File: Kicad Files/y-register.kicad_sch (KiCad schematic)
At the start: 20 parts, among them U1 74LS245, U2 74LS173, U3 74LS173

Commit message: updated library
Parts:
- removed D25, D26, D27, D28, D29, D30, D31, D32: RED, LED_THT:LED_D5.0mm, symbol 8bit-computer-rescue:LED_ALT-Device
- removed R25, R26, R27, R28, R29, R30, R31, R32: R, Resistor_THT:R_Axial_DIN0207_L6.3mm_D2.5mm_P7.62mm_Horizontal, symbol Device:R
- removed U1: 74LS245, Package_DIP:DIP-20_W7.62mm, symbol 8bit-computer-rescue:74LS245-8bit-computer-rescue
- removed U2, U3: 74LS173, Package_DIP:DIP-16_W7.62mm, symbol 8bit-computer-rescue:74LS173-8bit-computer-rescue
- added D33, D34, D35, D36, D37, D38, D39, D40: LED, symbol Device:LED
- added R33, R34, R35, R36, R37, R38, R39, R40: R_Small, symbol Device:R_Small
- added U1: 74HC245, symbol 74xx:74HC245
- added U2, U3: 74LS173, symbol 74xx:74LS173
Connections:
- net BUS_0: now also U1.11 (B7), U3.11 (D3)
- net BUS_1: now also U1.12 (B6), U3.12 (D2)
- net BUS_2: now also U1.13 (B5), U3.13 (D1)
- net BUS_3: now also U1.14 (B4), U3.14 (D0)
- net BUS_4: now also U1.15 (B3), U2.11 (D3)
- net BUS_5: now also U1.16 (B2), U2.12 (D2)
- net BUS_6: now also U1.17 (B1), U2.13 (D1)
- net BUS_7: now also U1.18 (B0), U2.14 (D0)
- net CLK: now also U2.7 (Cp), U3.7 (Cp)
- net CLR: now also U2.15 (Mr), U3.15 (Mr)
- net GND: now also R33.2, R34.2, R35.2, R36.2, R37.2, R38.2, R39.2, R40.2, U1.10 (GND), U2.1 (Oe1), U2.16 (VCC), U2.2 (Oe2), U3.1 (Oe1), U3.16 (VCC), U3.2 (Oe2)
- net VCC: now also U1.1 (A->B), U1.20 (VCC), U2.8 (GND), U3.8 (GND)
- net ~{YI}: now also U2.10 (E2), U2.9 (E1), U3.10 (E2), U3.9 (E1)
- net ~{YO}: now also U1.19 (CE)
- new net: D33.2 (A), U1.2 (A0), U2.3 (Q0)
- new net: D34.2 (A), U1.3 (A1), U2.4 (Q1)
- new net: D35.2 (A), U1.4 (A2), U2.5 (Q2)
- new net: D36.2 (A), U1.5 (A3), U2.6 (Q3)
- new net: D33.1 (K), R33.1
- new net: D35.1 (K), R35.1
- new net: D38.1 (K), R38.1
- new net: D38.2 (A), U1.7 (A5), U3.4 (Q1)
- new net: D37.1 (K), R37.1
- new net: D34.1 (K), R34.1
- new net: D36.1 (K), R36.1
- new net: D40.1 (K), R40.1
- new net: D37.2 (A), U1.6 (A4), U3.3 (Q0)
- new net: D40.2 (A), U1.9 (A7), U3.6 (Q3)
- new net: D39.2 (A), U1.8 (A6), U3.5 (Q2)
- new net: D39.1 (K), R39.1
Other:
- moved on the sheet: C2

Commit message: im sooo stupiiid
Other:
- moved on the sheet: C2, D33, D34, D35, D36, D37, D38, D39, D40, R33, R34, R35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

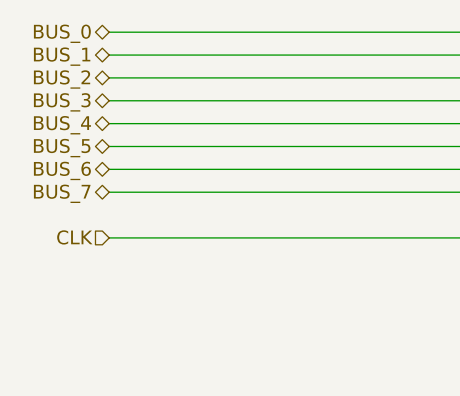
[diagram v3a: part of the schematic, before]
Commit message: complete redraw to bus system
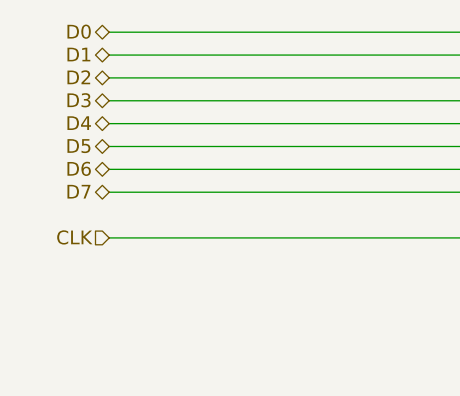
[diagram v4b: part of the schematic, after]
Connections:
- net BUS_0 renamed D0
- net BUS_1 renamed D1
- net BUS_2 renamed D2
- net BUS_3 renamed D3
- net BUS_4 renamed D4
- net BUS_5 renamed D5
- net BUS_6 renamed D6
- net BUS_7 renamed D7
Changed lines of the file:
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@@
     (stroke (width 0) (type default) (color 0 0 0 0))
   )
-  (hierarchical_label "BUS_3" (shape bidirectional) (at 55.88 46.99 180)
-    (effects (font (size 1.524 1.524)) (justify right))
-  )
-  (hierarchical_label "BUS_7" (shape bidirectional) (at 55.88 57.15 180)
+  (hierarchical_label "D3" (shape tri_state) (at 55.88 46.99 180)
     (effects (font (size 1.524 1.524)) (justify right))
   )
@@
     (effects (font (size 1.524 1.524)) (justify left))
   )
-  (hierarchical_label "BUS_5" (shape bidirectional) (at 55.88 52.07 180)
+  (hierarchical_label "D1" (shape tri_state) (at 55.88 41.91 180)
     (effects (font (size 1.524 1.524)) (justify right))
   )
-  (hierarchical_label "BUS_4" (shape bidirectional) (at 55.88 49.53 180)
+  (hierarchical_label "D6" (shape tri_state) (at 55.88 54.61 180)
     (effects (font (size 1.524 1.524)) (justify right))
   )
-  (hierarchical_label "BUS_1" (shape bidirectional) (at 55.88 41.91 180)
+  (hierarchical_label "D7" (shape tri_state) (at 55.88 57.15 180)
     (effects (font (size 1.524 1.524)) (justify right))
   )
-  (hierarchical_label "BUS_0" (shape bidirectional) (at 55.88 39.37 180)
+  (hierarchical_label "D5" (shape tri_state) (at 55.88 52.07 180)
     (effects (font (size 1.524 1.524)) (justify right))
   )
-  (hierarchical_label "BUS_2" (shape bidirectional) (at 55.88 44.45 180)
+  (hierarchical_label "D4" (shape tri_state) (at 55.88 49.53 180)
     (effects (font (size 1.524 1.524)) (justify right))
   )
-  (hierarchical_label "BUS_6" (shape bidirectional) (at 55.88 54.61 180)
+  (hierarchical_label "D2" (shape tri_state) (at 55.88 44.45 180)
     (effects (font (size 1.524 1.524)) (justify right))
   )
+  (hierarchical_label "D0" (shape tri_state) (at 55.88 39.37 180)
+    (effects (font (size 1.524 1.524)) (justify right))
+  )
